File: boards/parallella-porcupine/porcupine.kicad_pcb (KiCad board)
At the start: 2 copper layers, 86.4 x 54.6 mm, 29 parts, among them J1 CONN\HDR\P1\1R02, J10 CONN\HDR\P1\1R04, J11 CONN\HDR\2MM\2R07\SHD, J12 CONN\HDR\P1\1R02, J13 CONN\HDR\P1\1R02, J14 CONN\HDR\P1\2R15\SHD, J15 CONN\HDR\P1\2R15\SHD, J16 CONN\HDR\P1\2R15\SHD, J17 CONN\HDR\P1\1R15, J18 CONN\HDR\P1\1R15, J19 CONN\HDR\P1\2R15\SHD, J2 CONN\HDR\P1\1R02, J20 CONN\HDR\P1\2R15\SHD, J3 CONN\HDR\P1\2R15\SHD, J4 CONN\HDR\P1\2R15\SHD, J5 CONN\HDR\P1\1R08, J6 CONN\HDR\P1\2R08, J7 CONN\HDR\P1\2R08, J8 CONN\HDR\P1\1R04, J9 CONN\HDR\P1\1R04, P1 CONN\SAMTEC\BTH\60, P2 CONN\SAMTEC\BTH\60, P3 CONN\SAMTEC\BTH\60, P4 CONN\SAMTEC\BTH\60

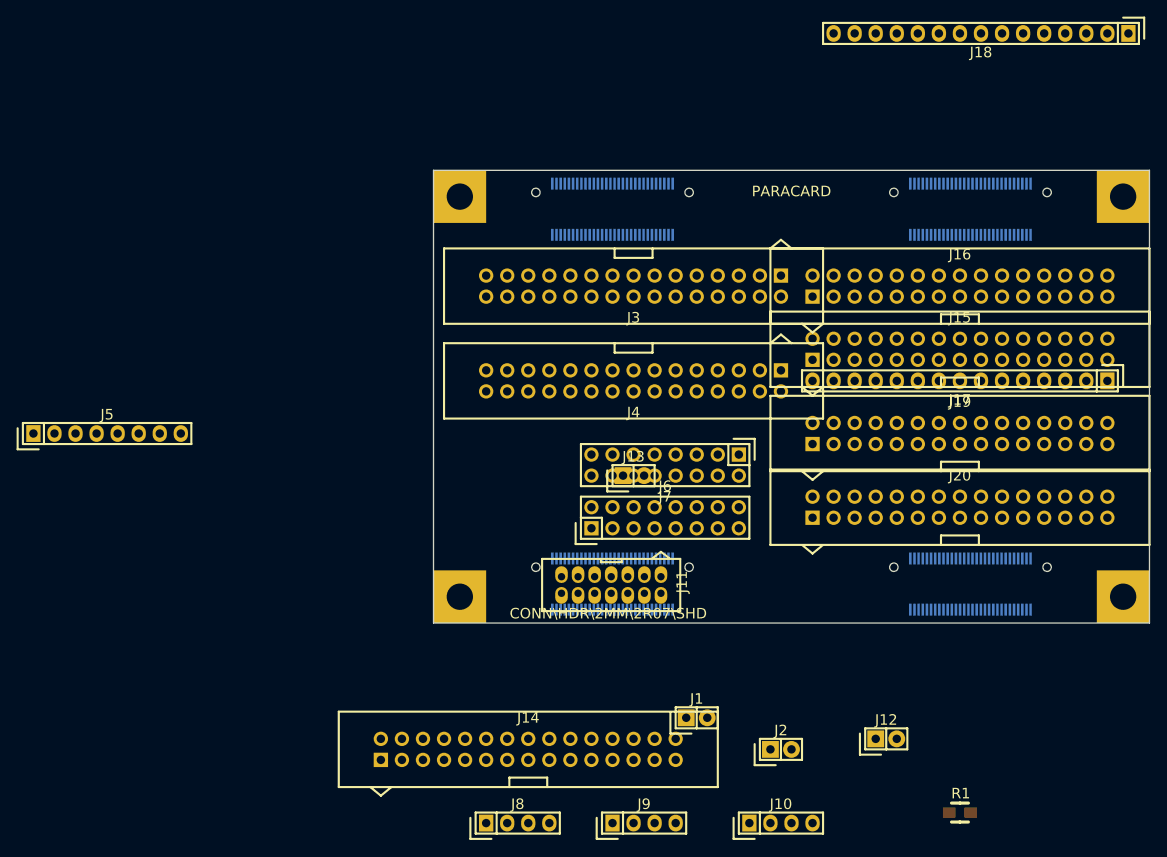
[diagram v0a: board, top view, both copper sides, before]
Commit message: Schematic is stable, PCB mostly routed.
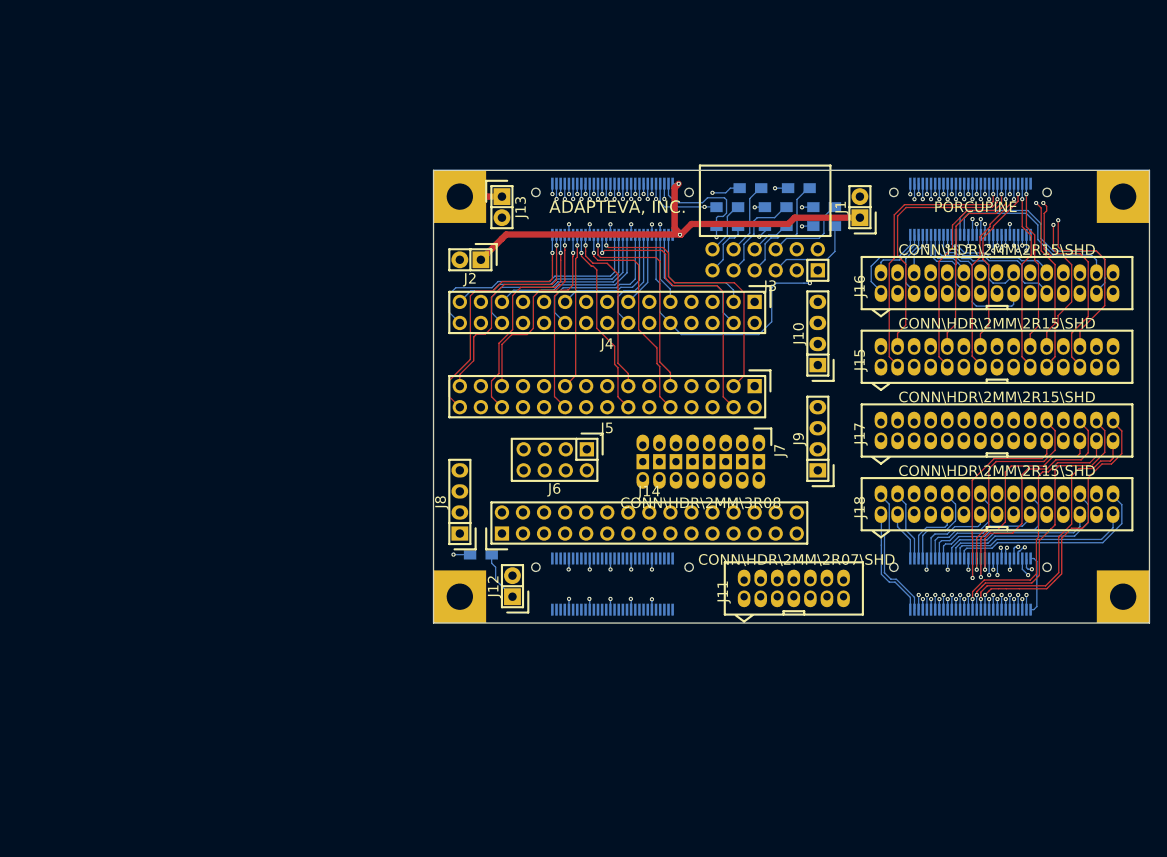
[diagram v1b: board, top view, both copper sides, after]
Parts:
- removed J19, J20: CONN\HDR\P1\2R15\SHD, CONN_HDR_P1_2R15_SHD
- removed the J8 at (162.6, 180.3)
- added J10: CONN\HDR\P1\1R04, Adapteva:CONN_HDR_P1_1R04, F.Cu at (198.8, 121.3)
- added R2: 200, R_0805_HS, B.Cu at (193.7, 108.3)
- added R3: 200, R_0805_HS, B.Cu at (190.6, 103.8)
- added R4: 200, R_0805_HS, B.Cu at (187.8, 106.0)
- added R5: 200, R_0805_HS, B.Cu at (199.5, 108.3)
- added R6: 200, R_0805_HS, B.Cu at (196.5, 103.8)
- added R7: 200, R_0805_HS, B.Cu at (193.7, 106.0)
- added R8: 200, R_0805_HS, B.Cu at (187.8, 108.3)
- added R9: 1K, R_0805_HS, B.Cu at (158.1, 148.0)
- J1, J12, J13, J2: footprint CONN_HDR_P1_1R02 -> Adapteva:CONN_HDR_P1_1R02
- J14, J4: value CONN\HDR\P1\2R15\SHD -> CONN\HDR\P1\2R15; footprint CONN_HDR_P1_2R15_SHD -> CONN_HDR_P1_2R15
- J15, J16: value CONN\HDR\P1\2R15\SHD -> CONN\HDR\2MM\2R15\SHD; footprint CONN_HDR_P1_2R15_SHD -> Adapteva:CONN_HDR_2MM_2R15_SHD
- J17, J18: value CONN\HDR\P1\1R15 -> CONN\HDR\2MM\2R15\SHD; footprint CONN_HDR_P1_1R15 -> Adapteva:CONN_HDR_2MM_2R15_SHD
- J3: value CONN\HDR\P1\2R15\SHD -> CONN\HDR\P1FRA\2R06; footprint CONN_HDR_P1_2R15_SHD -> CONN_HDR_P1FRA_2R06
- J5: value CONN\HDR\P1\1R08 -> CONN\HDR\P1\2R15; footprint CONN_HDR_P1_1R08 -> CONN_HDR_P1_2R15
- J6: value CONN\HDR\P1\2R08 -> CONN\HDR\P1\2R04; footprint CONN_HDR_P1_2R08 -> CONN_HDR_P1_2R04
- J7: value CONN\HDR\P1\2R08 -> CONN\HDR\2MM\3R08; footprint CONN_HDR_P1_2R08 -> CONN_HDR_2MM_3R08
- J8: renamed from J10; footprint CONN_HDR_P1_1R04 -> Adapteva:CONN_HDR_P1_1R04
- J9: footprint CONN_HDR_P1_1R04 -> Adapteva:CONN_HDR_P1_1R04
- P1, P2, P3, P4: footprint CONN_SAMTEC_BTH_60 -> Adapteva:CONN_SAMTEC_BTH_60
- R1: value 1K -> 200; moved to B.Cu
- moved R1 74.8 mm to (199.5, 106.0)
- moved J2 69.9 mm to (156.8, 112.4), turned to 180 degrees
- moved J1 64.7 mm to (203.8, 106.0), turned to 90 degrees
- moved J5 60.5 mm to (173.4, 128.9), turned to 180 degrees
- moved J18 59.0 mm to (206.4, 142.9), turned to 0 degrees
- moved J8 54.8 mm to (155.6, 141.6), turned to 90 degrees
- moved J9 50.9 mm to (198.8, 134.0), turned to 90 degrees
- moved J12 48.7 mm to (161.9, 151.8), turned to 90 degrees
- moved J13 36.1 mm to (160.7, 106.0), turned to 270 degrees
- moved J14 31.0 mm to (178.4, 144.1)
- moved J3 16.2 mm to (192.4, 112.4)
- moved J6 15.1 mm to (167.0, 136.5), turned to 180 degrees
- moved J17 11.8 mm to (206.4, 134.0), turned to 0 degrees
- moved J7 11.6 mm to (191.6, 134.7)
- moved J11 10.3 mm to (189.9, 153.0), turned to 0 degrees
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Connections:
- J17 pad 1: /NORTH/RXI_DATA_P7 -> /P_ELINK_S/RXI_DATA_P7
- J17 pad 10: /NORTH/RXI_DATA_P0 -> /P_ELINK_S/RXI_DATA_N4
- J17 pad 11: /NORTH/RXO_RD_WAIT_P -> /P_ELINK_S/RXI_DATA_P3
- J17 pad 12: GND -> /P_ELINK_S/RXI_DATA_N3
- J17 pad 13: /NORTH/RXI_LCLK_P -> /P_ELINK_S/RXI_DATA_P2
- J17 pad 14: /NORTH/RXO_WR_WAIT_P -> /P_ELINK_S/RXI_DATA_N2
- J17 pad 15: /NORTH/RXI_FRAME_P -> GND
- J17 pad 2: /NORTH/RXI_DATA_P6 -> /P_ELINK_S/RXI_DATA_N7
- J17 pad 3: /NORTH/RXI_DATA_P5 -> /P_ELINK_S/RXI_DATA_P6
- J17 pad 4: GND -> /P_ELINK_S/RXI_DATA_N6
- J17 pad 5: /NORTH/RXI_DATA_P4 -> /P_ELINK_S/RXI_DATA_P5
- J17 pad 6: /NORTH/RXI_DATA_P3 -> /P_ELINK_S/RXI_DATA_N5
- J17 pad 7: /NORTH/RXI_DATA_P2 -> GND
- J17 pad 9: /NORTH/RXI_DATA_P1 -> /P_ELINK_S/RXI_DATA_P4
- J18 pad 1: /NORTH/TXO_DATA_P7 -> /P_ELINK_S/TXO_DATA_P7
- J18 pad 10: /NORTH/TXO_DATA_P0 -> /P_ELINK_S/TXO_DATA_N4
- J18 pad 11: /NORTH/TXI_RD_WAIT_P -> /P_ELINK_S/TXO_DATA_P3
- J18 pad 12: GND -> /P_ELINK_S/TXO_DATA_N3
- J18 pad 13: /NORTH/TXO_LCLK_P -> /P_ELINK_S/TXO_DATA_P2
- J18 pad 14: /NORTH/TXI_WR_WAIT_P -> /P_ELINK_S/TXO_DATA_N2
- J18 pad 15: /NORTH/TXO_FRAME_P -> GND
- J18 pad 2: /NORTH/TXO_DATA_P6 -> /P_ELINK_S/TXO_DATA_N7
- J18 pad 3: /NORTH/TXO_DATA_P5 -> /P_ELINK_S/TXO_DATA_P6
- J18 pad 4: GND -> /P_ELINK_S/TXO_DATA_N6
- J18 pad 5: /NORTH/TXO_DATA_P4 -> /P_ELINK_S/TXO_DATA_P5
- J18 pad 6: /NORTH/TXO_DATA_P3 -> /P_ELINK_S/TXO_DATA_N5
- J18 pad 7: /NORTH/TXO_DATA_P2 -> GND
- J18 pad 9: /NORTH/TXO_DATA_P1 -> /P_ELINK_S/TXO_DATA_P4
- J3 pad 1: /GPIO/GPIO0 -> /POWER/3P3V
- J3 pad 10: /GPIO/GPIO7 -> /P_GPIO/PMOD22
- J3 pad 11: /GPIO/GPIO8 -> /P_GPIO/PMOD11
- J3 pad 12: /GPIO/GPIO10 -> /P_GPIO/PMOD21
- J3 pad 2: /GPIO/GPIO2 -> /POWER/3P3V
- J3 pad 3: /GPIO/GPIO1 -> GND
- J3 pad 4: /GPIO/GPIO3 -> GND
- J3 pad 5: /GPIO/GPIO4 -> /P_GPIO/PMOD14
- J3 pad 6: /GPIO/GPIO6 -> /P_GPIO/PMOD24
- J3 pad 7: GND -> /P_GPIO/PMOD13
- J3 pad 8: GND -> /P_GPIO/PMOD23
- J3 pad 9: /GPIO/GPIO5 -> /P_GPIO/PMOD12
- J4 pad 1: /GPIO/GPIO24 -> /GPIO/GPIO0
- J4 pad 10: /GPIO/GPIO31 -> /GPIO/GPIO7
- J4 pad 11: /GPIO/GPIO32 -> /GPIO/GPIO8
- J4 pad 12: /GPIO/GPIO34 -> /GPIO/GPIO10
- J4 pad 13: /GPIO/GPIO33 -> /GPIO/GPIO9
- J4 pad 14: /GPIO/GPIO35 -> /GPIO/GPIO11
- J4 pad 17: /GPIO/GPIO36 -> /GPIO/GPIO12
- J4 pad 18: /GPIO/GPIO38 -> /GPIO/GPIO14
- J4 pad 19: /GPIO/GPIO37 -> /GPIO/GPIO13
- J4 pad 2: /GPIO/GPIO26 -> /GPIO/GPIO2
- J4 pad 20: /GPIO/GPIO39 -> /GPIO/GPIO15
- J4 pad 21: /GPIO/GPIO40 -> /GPIO/GPIO16
- J4 pad 22: /GPIO/GPIO42 -> /GPIO/GPIO18
- J4 pad 25: /GPIO/GPIO41 -> /GPIO/GPIO17
- J4 pad 26: /GPIO/GPIO43 -> /GPIO/GPIO19
- J4 pad 27: /GPIO/GPIO44 -> /GPIO/GPIO20
- J4 pad 28: /GPIO/GPIO46 -> /GPIO/GPIO22
- J4 pad 29: /GPIO/GPIO45 -> /GPIO/GPIO21
- J4 pad 3: /GPIO/GPIO25 -> /GPIO/GPIO1
- J4 pad 30: /GPIO/GPIO47 -> /GPIO/GPIO23
- J4 pad 4: /GPIO/GPIO27 -> /GPIO/GPIO3
- J4 pad 5: /GPIO/GPIO28 -> /GPIO/GPIO4
- J4 pad 6: /GPIO/GPIO30 -> /GPIO/GPIO6
- J4 pad 9: /GPIO/GPIO29 -> /GPIO/GPIO5
- J5 pad 1: /POWER/1P8V -> /GPIO/GPIO24
- J5 pad 2: /POWER/1P8V -> /GPIO/GPIO26
- J5 pad 3: /POWER/1P8V -> /GPIO/GPIO25
- J5 pad 4: /POWER/1P8V -> /GPIO/GPIO27
- J5 pad 5: /POWER/1P8V -> /GPIO/GPIO28
- J5 pad 6: /POWER/1P8V -> /GPIO/GPIO30
- J5 pad 7: /POWER/1P8V -> GND
- J5 pad 8: /POWER/1P8V -> GND
- J6 pad 2: GND -> /POWER/RESET_N
- J6 pad 3: /POWER/RESET_N -> /POWER/DSP_FLAG
- J6 pad 4: GND -> /POWER/USER_LED
- J6 pad 5: /POWER/DSP_FLAG -> /POWER/PROG_IO
- J6 pad 6: GND -> /POWER/TURBO_MODE
- J6 pad 7: /POWER/USER_LED -> /POWER/SPDIF
- J7 pad 1: /POWER/DSP_YID0 -> /POWER/1P8V
- J7 pad 10: GND -> /POWER/1P8V
- J7 pad 11: /POWER/DSP_XID1 -> /POWER/DSP_YID3
- J7 pad 13: /POWER/DSP_XID2 -> /POWER/1P8V
- J7 pad 14: GND -> /POWER/DSP_XID0
- J7 pad 15: /POWER/DSP_XID3 -> GND
- J7 pad 16: GND -> /POWER/1P8V
- J7 pad 2: GND -> /POWER/DSP_YID0
- J7 pad 3: /POWER/DSP_YID1 -> GND
- J7 pad 4: GND -> /POWER/1P8V
- J7 pad 5: /POWER/DSP_YID2 -> /POWER/DSP_YID1
- J7 pad 7: /POWER/DSP_YID3 -> /POWER/1P8V
- J7 pad 8: GND -> /POWER/DSP_YID2
- J7 pad 9: /POWER/DSP_XID0 -> GND
- J8 pad 2: /POWER/UART_RX -> /POWER/VADC_P
- J8 pad 3: /POWER/UART_TX -> /POWER/VADC_N
- R1 pad 1: Net-(J12-Pad1) -> /GPIO/GPIO7
- R1 pad 2: GND -> /P_GPIO/PMOD24
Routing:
- net GND: track 0.00 -> 58.7 mm, vias 0 -> 41
- net /P_GPIO/VDD_GPIO: track 0.00 -> 56.4 mm, vias 0 -> 2
- net /GPIO/GPIO7: track 0.00 -> 47.8 mm, vias 0 -> 2
- net /GPIO/GPIO26: track 0.00 -> 43.3 mm, vias 0 -> 1
- net /GPIO/GPIO24: track 0.00 -> 42.5 mm, vias 0 -> 1
- net /GPIO/GPIO3: track 0.00 -> 39.5 mm, vias 0 -> 1
- net /GPIO/GPIO30: track 0.00 -> 39.1 mm, vias 0 -> 1
- net /GPIO/GPIO28: track 0.00 -> 38.2 mm, vias 0 -> 1
- net /P_ELINK_S/RXI_DATA_N7: track 0.00 -> 37.5 mm, vias 0 -> 1
- net /GPIO/GPIO46: track 0.00 -> 36.9 mm, vias 0 -> 1
- net /GPIO/GPIO6: track 0.00 -> 36.7 mm, vias 0 -> 2
- net /GPIO/GPIO2: track 0.00 -> 36.6 mm, vias 0 -> 2
- net /NORTH/RXO_RD_WAIT_P: track 0.00 -> 36.5 mm, vias 0 -> 2
- net /P_ELINK_S/RXO_WR_WAIT_N: track 0.00 -> 35.4 mm, vias 0 -> 1
- net /P_ELINK_S/RXI_FRAME_N: track 0.00 -> 35.2 mm, vias 0 -> 1
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- added copper zone on Inner1.Cu, net GND
- added copper zone on Inner4.Cu, net GND
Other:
- copper layers 2 -> 6
- net class Default: via_dia 0.889 -> 0.508; via_drill 0.508 -> 0.254
- rule pad_to_mask_clearance: 0 -> 0.127
- rule via_min_drill: 0.508 -> 0.254
- rule via_min_size: 0.889 -> 0.508
- board text added: "ADAPTEVA, INC."
- board text added: "PORCUPINE"
- board text removed: "PARACARD"

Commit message: Fully routed design, needs checks, drill dwg.  Removed elink-north/south as these are now the same.
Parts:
- turned J13 to 90 degrees
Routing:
- net /POWER/UART_TX: track 0.00 -> 62.3 mm, vias 0 -> 1
- net /POWER/UART_RX: track 0.00 -> 58.4 mm, vias 0 -> 1
- net /POWER/JTAG_TDI: track 0.00 -> 35.8 mm, vias 0 -> 1
- net /POWER/JTAG_TDO: track 0.00 -> 34.5 mm, vias 0 -> 1
- net /POWER/I2C_SCL: track 0.00 -> 32.5 mm
- net /POWER/I2C_SDA: track 0.00 -> 32.3 mm
- net /POWER/JTAG_TCK: track 0.00 -> 30.7 mm, vias 0 -> 1
- net /POWER/JTAG_TMS: track 0.00 -> 28.7 mm, vias 0 -> 1
- net /POWER/VADC_N: track 0.00 -> 27.4 mm, vias 0 -> 1
- net /POWER/DSP_YID0: track 0.00 -> 26.8 mm, vias 0 -> 1
- net /POWER/VADC_P: track 0.00 -> 26.7 mm, vias 0 -> 1
- net /POWER/DSP_YID1: track 0.00 -> 25.6 mm, vias 0 -> 1
- net /POWER/DSP_YID2: track 0.00 -> 24.9 mm, vias 0 -> 1
- net /POWER/1P0V: track 0.00 -> 23.8 mm, vias 0 -> 1
- net /POWER/USER_LED: track 0.00 -> 23.6 mm, vias 0 -> 1
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- added copper zone on Inner1.Cu, net /POWER/1P8V
- added copper zone on Inner1.Cu, net /POWER/3P3V
- added copper zone on Inner1.Cu, net /POWER/SYS_5P0V
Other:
- board text added: "fh"

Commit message: Completed design w/3-row XID/YID and various 4-pin IO connectors. Fixed page ordering, changed "Mfr" field to "Manufacturer" Will now re-do to combine all misc. functions onto a single 2xN connector.
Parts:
- added FID1: FIDUCIAL\040, Adapteva:FIDUCIAL_040, B.Cu at (234.3, 148.0)
- added FID2: FIDUCIAL\040, Adapteva:FIDUCIAL_040, B.Cu at (155.6, 134.0)
- added FID3: FIDUCIAL\040, Adapteva:FIDUCIAL_040, B.Cu at (230.5, 107.3)
- added FID4: FIDUCIAL\040, Adapteva:FIDUCIAL_040, F.Cu at (234.3, 148.0)
- added FID5: FIDUCIAL\040, Adapteva:FIDUCIAL_040, F.Cu at (155.6, 134.0)
- added FID6: FIDUCIAL\040, Adapteva:FIDUCIAL_040, F.Cu at (230.5, 107.3)
- MH1, MH2, MH3, MH4: footprint MTG_PTH_125_SQ -> Adapteva:MTG_PTH_125_SQ
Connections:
- J11 pad 1: Net-(J11-Pad1) -> (no net)
- J11 pad 12: Net-(J11-Pad12) -> (no net)
- J11 pad 14: Net-(J11-Pad14) -> (no net)
- J14 pad 17: Net-(J14-Pad17) -> (no net)
- P3 pad 10: Net-(P3-Pad10) -> (no net)
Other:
- rule pad_to_mask_clearance: 0.127 -> 0.0762
- board text added: "5 G"
- board text added: "G VG"
- board text added: "GND SCL SDA 5V"
- board text added: "GND TX RX 3.3V"
- board text added: "GPIO A"
- board text added: "GPIO B"
- board text added: "JTAG"
- board text added: "MADE IN U.S.A."
- board text added: "NORTH RX"
- board text added: "NORTH TX"
- board text added: "NOT RELEASED FOR MANUFACTURE"
- board text added: "P N G ADC"
- board text added: "PMOD"
- board text added: "SOUTH RX"
- board text added: "SOUTH TX"
- board text added: "VG G"
- board text added: "X3210 Y3210"

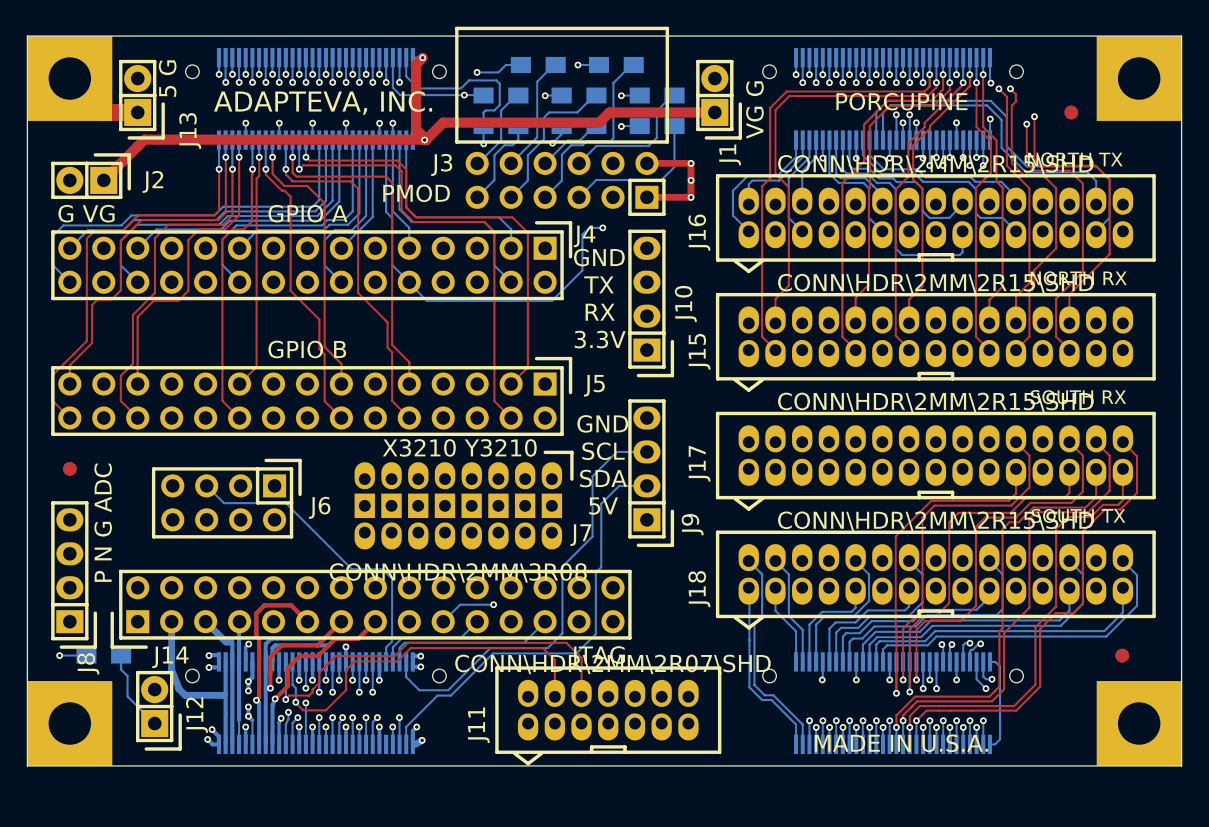
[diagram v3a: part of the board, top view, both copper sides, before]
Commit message: Changed to a single header for all the PEC_POWER/misc. stuff. Added 3D models for shrouded & right-angle connectors.
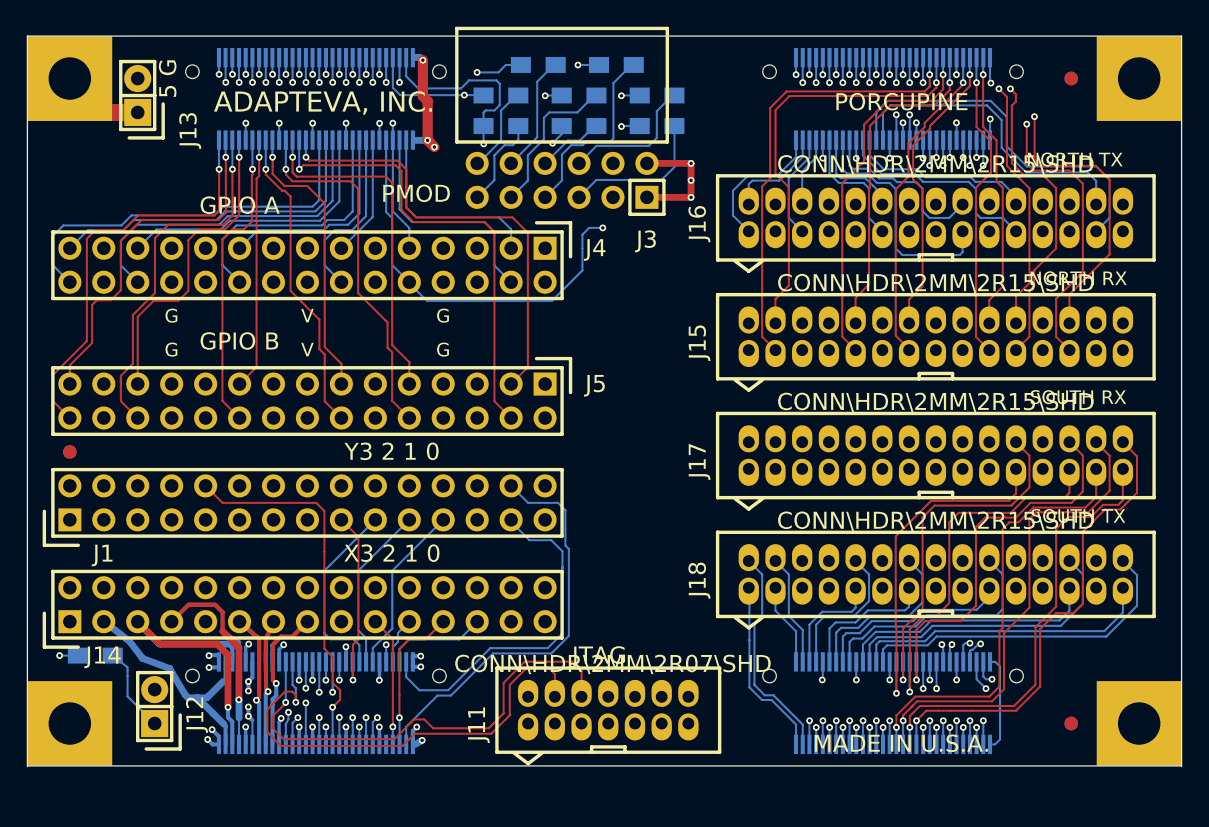
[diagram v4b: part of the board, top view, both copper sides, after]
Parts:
- removed J10, J8, J9: CONN\HDR\P1\1R04, Adapteva:CONN_HDR_P1_1R04
- removed J2: CONN\HDR\P1\1R02, Adapteva:CONN_HDR_P1_1R02
- removed J6: CONN\HDR\P1\2R04, CONN_HDR_P1_2R04
- removed J7: CONN\HDR\2MM\3R08, CONN_HDR_2MM_3R08
- J1: value CONN\HDR\P1\1R02 -> CONN\HDR\P1\2R15; footprint Adapteva:CONN_HDR_P1_1R02 -> CONN_HDR_P1_2R15
- J11: footprint CONN_HDR_2MM_2R07_SHD -> Adapteva:CONN_HDR_2MM_2R07_SHD
- J3: footprint CONN_HDR_P1FRA_2R06 -> Adapteva:CONN_HDR_P1FRA_2R06
- R9: value 1K -> 1k00
- moved J1 43.1 mm to (173.4, 136.5), turned to 0 degrees
- moved FID1 6.35 mm to (230.5, 153.0)
- moved FID4 6.35 mm to (230.5, 153.0)
- moved J14 5.08 mm to (173.4, 144.1)
- moved FID3 2.54 mm to (230.5, 104.8)
- moved FID6 2.54 mm to (230.5, 104.8)
- moved FID2 1.27 mm to (155.6, 132.7)
- moved FID5 1.27 mm to (155.6, 132.7)
- moved R9 0.64 mm to (157.5, 148.0)
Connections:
- J1 pad 1: /P_GPIO/VDD_GPIO -> /POWER/VADC_N
- J1 pad 2: GND -> /POWER/VADC_P
- J4 pad 15: GND -> /P_GPIO/VDD_GPIO
- J4 pad 16: GND -> /P_GPIO/VDD_GPIO
- J5 pad 15: GND -> /P_GPIO/VDD_GPIO
- J5 pad 16: GND -> /P_GPIO/VDD_GPIO
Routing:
- net /POWER/UART_TX: track 62.3 -> 27.8 mm
- net /POWER/UART_RX: track 58.4 -> 29.6 mm
- net /P_GPIO/VDD_GPIO: track 56.4 -> 40.0 mm, vias 2 -> 3
- net /POWER/VDD_ADJ: track 9.20 -> 23.9 mm, vias 0 -> 1
- net /POWER/VDD_GPIO: track 10.2 -> 23.6 mm, vias 0 -> 1
- net /POWER/REG_EN4: track 21.6 -> 9.72 mm, vias 2 -> 1
- net /POWER/RESET_N: track 19.8 -> 31.0 mm
- net /POWER/VDD_DSP: track 23.0 -> 12.6 mm
- net /POWER/VADC_P: track 26.7 -> 36.1 mm
- net /POWER/1P35V: track 22.9 -> 13.7 mm
- net /POWER/USER_LED: track 23.6 -> 32.7 mm
- net /POWER/1P0V: track 23.8 -> 15.6 mm
- net /POWER/JTAG_TMS: track 28.7 -> 35.8 mm
- net /POWER/DSP_XID0: track 19.6 -> 12.8 mm, vias 1 -> 0
- net /POWER/I2C_SCL: track 32.5 -> 26.2 mm
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- added copper zone on Inner2.Cu, net /POWER/VDD_ADJ
- added copper zone on Inner1.Cu, net /POWER/VDD_GPIO
- added copper zone on Inner2.Cu, net /P_GPIO/VDD_GPIO
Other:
- board text added: "G"
- board text added: "V"
- board text added: "X3 2 1 0"
- board text added: "Y3 2 1 0"
- board text removed: "G VG"
- board text removed: "GND SCL SDA 5V"
- board text removed: "GND TX RX 3.3V"
- board text removed: "P N G ADC"
- board text removed: "VG G"
- board text removed: "X3210 Y3210"
